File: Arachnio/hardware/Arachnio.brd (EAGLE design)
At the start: 17.8 x 58.4 mm, 64 parts, among them J5 HEAD17-NOSS, J6 HEAD17-NOSS, Q1 8MHz, T1 FDN340P/PMV48XP, U1 ATMEGA32U4-XUMU, U2 AP2111HA-3.3, U3 ZLDO1117-5.0, U5 ESP8266EX, U6 SPI_FLASH, Y1 26 MHz/10 pF

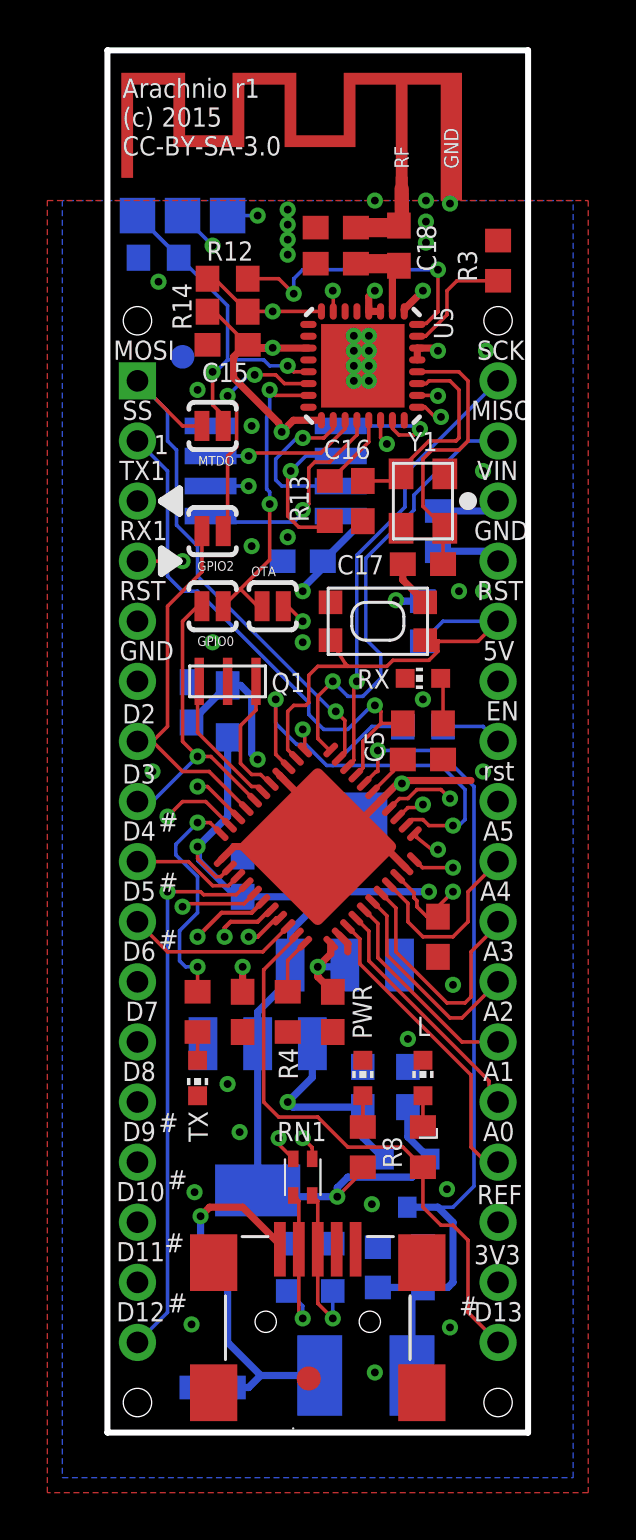
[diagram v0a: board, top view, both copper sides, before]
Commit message: -- Fixed missing parts designators in silkscreen
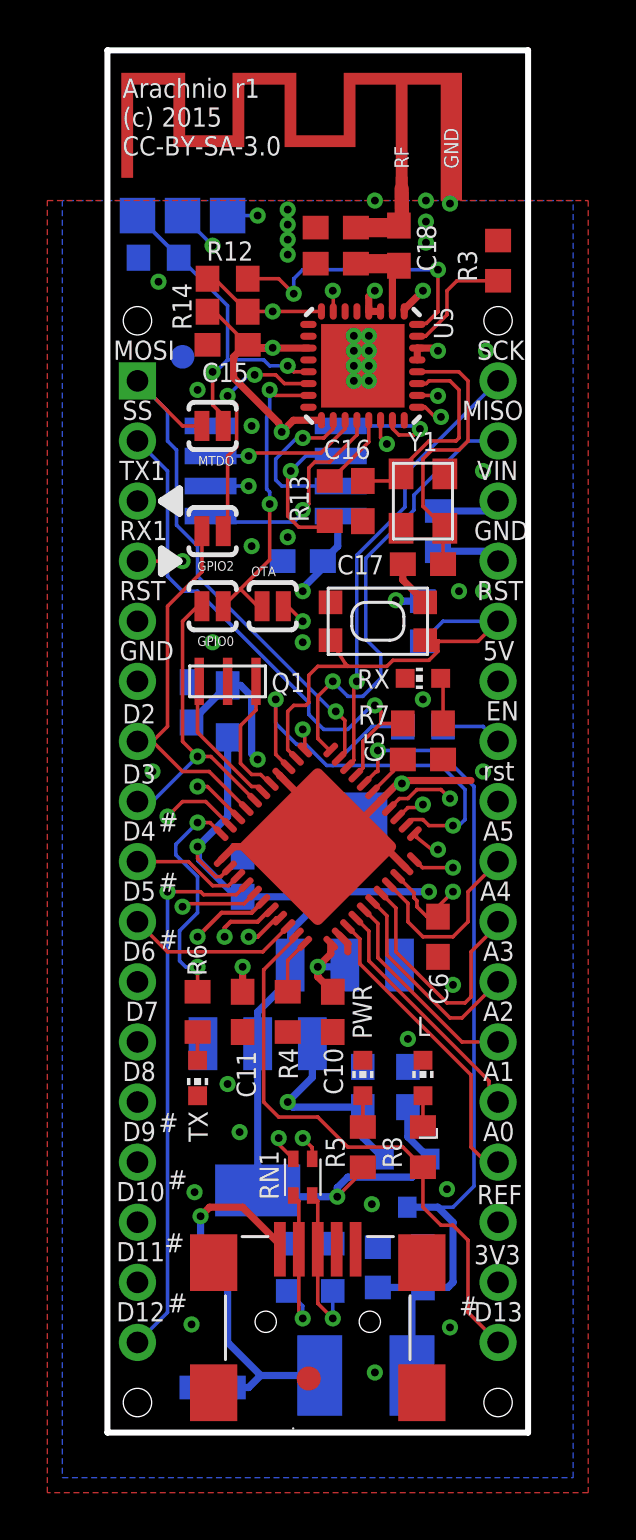
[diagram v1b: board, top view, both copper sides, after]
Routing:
- net 3V3: track 68.4 -> 66.9 mm
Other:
- board text removed: "1"

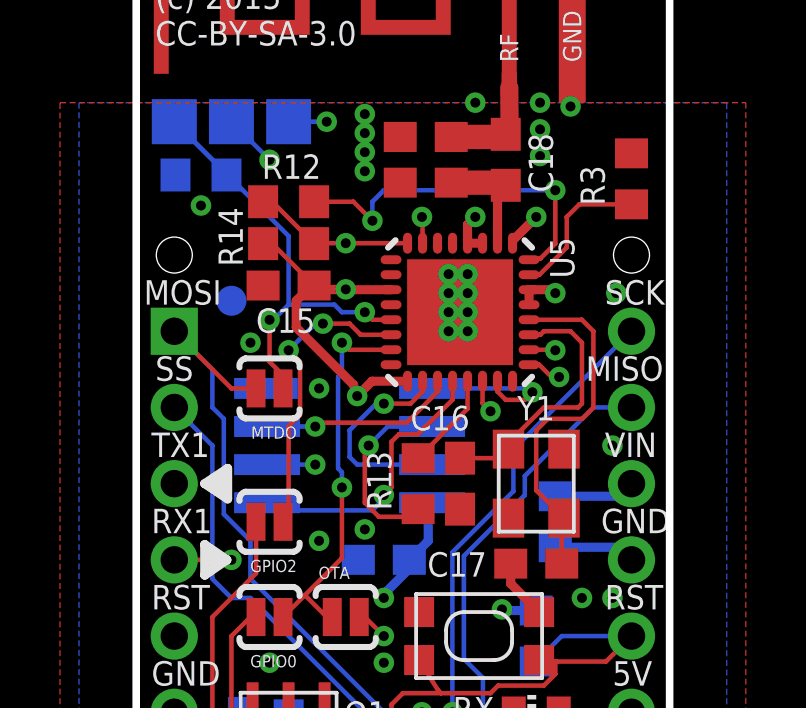
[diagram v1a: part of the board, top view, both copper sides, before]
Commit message: ﻿Added 3 new decoupling caps to the ESP8266 # Please enter the commit message for your changes. Lines starting # with '#' will be ignored, and an empty message aborts the commit. # On branch decoupling # Changes to be committed: #	modified:   Arachnio/hardware/Arachnio.brd #	modified:   Arachnio/hardware/Arachnio.sch #
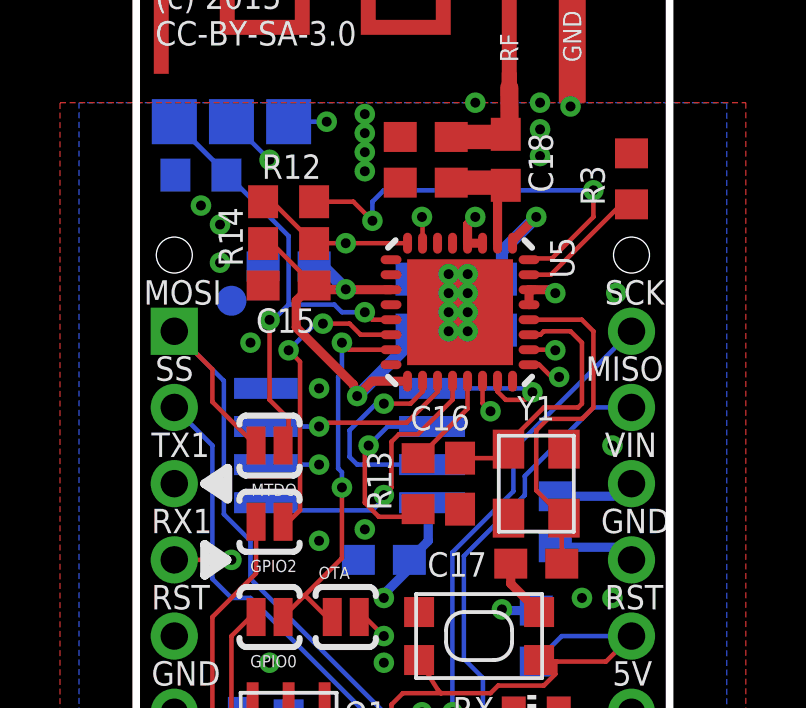
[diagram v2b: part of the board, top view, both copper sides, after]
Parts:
- added C12, C13: 100n, resistor:C0603
- added C2: 1u, resistor:C0603
- moved MTDO 1.91 mm to (4.45, 40.6)
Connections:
- net 3V3: now also C12.1, C13.1, C2.1
- net GND: now also C12.2, C13.2, C2.2
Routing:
- net 3V3: track 66.9 -> 73.7 mm
- net N$33: track 12.0 -> 14.0 mm
- net N$1: track 17.3 -> 19.2 mm
- net MOSI: track 23.3 -> 24.7 mm
- net GND: vias 38 -> 40
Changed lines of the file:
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@@
 <attribute name="BOM" value="EXCLUDE" x="4.445" y="38.1" size="1.778" layer="27" rot="R180" display="off"/>
 </element>
-<element name="MTDO" library="SparkFun-Passives" package="PAD-JUMPER-2-NO_YES_SILK" value="JUMPER-PAD-2-NOYES_SILK" x="4.445" y="42.545" rot="R180">
-<attribute name="BOM" value="EXCLUDE" x="4.445" y="42.545" size="1.778" layer="27" rot="R180" display="off"/>
+<element name="MTDO" library="SparkFun-Passives" package="PAD-JUMPER-2-NO_YES_SILK" value="JUMPER-PAD-2-NOYES_SILK" x="4.445" y="40.64" rot="R180">
+<attribute name="BOM" value="EXCLUDE" x="4.445" y="40.64" size="1.778" layer="27" rot="R180" display="off"/>
 </element>
 <element name="OTA" library="SparkFun-Passives" package="PAD-JUMPER-2-NO_YES_SILK" value="JUMPER-PAD-2-NOYES_SILK" x="6.985" y="34.925">
@@
 <element name="U$1" library="logos-faves" package="LOGO-SM" value="" x="17.145" y="46.99" rot="MR0"/>
 <element name="U$12" library="SparkFun-Aesthetics" package="OSHW-LOGO-S" value="" x="3.175" y="53.975" rot="MR0"/>
+<element name="C2" library="resistor" package="C0603" value="1u" x="5.08" y="46.609" rot="MR0">
+<attribute name="PARTNO" value="C0603C105K3PACTU" x="5.08" y="46.609" size="1.778" layer="28" rot="MR0" display="off"/>
+</element>
+<element name="C12" library="resistor" package="C0603" value="100n" x="9.144" y="45.339" rot="MR90">
+<attribute name="PARTNO" value="CC0603ZRY5V9BB104" x="9.144" y="45.339" size="1.778" layer="28" rot="MR90" display="off"/>
+</element>
+<element name="C13" library="resistor" package="C0603" value="100n" x="12.192" y="45.339" rot="MR270">
+<attribute name="PARTNO" value="CC0603ZRY5V9BB104" x="12.192" y="45.339" size="1.778" layer="28" rot="MR270" display="off"/>
+</element>
 </elements>
 <signals>
@@
 <wire x1="9.735" y1="38.73" x2="9.735" y2="37.46" width="0.3048" layer="16"/>
 <wire x1="9.735" y1="37.46" x2="9.105" y2="36.83" width="0.3048" layer="16"/>
+<contactref element="C2" pad="1"/>
+<contactref element="C12" pad="1"/>
+<contactref element="C13" pad="1"/>
+<wire x1="12.192" y1="46.189" x2="12.192" y2="47.117" width="0.4064" layer="16"/>
+<wire x1="12.192" y1="47.117" x2="13.335" y2="48.26" width="0.4064" layer="16"/>
+<wire x1="9.144" y1="44.489" x2="9.144" y2="44.069" width="0.4064" layer="16"/>
+<wire x1="9.144" y1="44.069" x2="7.366" y2="42.291" width="0.4064" layer="16"/>
+<wire x1="5.93" y1="46.609" x2="6.223" y2="46.609" width="0.4064" layer="16"/>
+<wire x1="6.223" y1="46.609" x2="6.985" y2="45.847" width="0.4064" layer="16"/>
 </signal>
 <signal name="D0/RX">
@@
 <via x="11.049" y="44.45" extent="1-16" drill="0.3302"/>
 <via x="10.414" y="44.45" extent="1-16" drill="0.3302"/>
+<contactref element="C2" pad="2"/>
+<contactref element="C12" pad="2"/>
+<contactref element="C13" pad="2"/>
+<via x="2.794" y="48.006" extent="1-16" drill="0.3302"/>
+<via x="2.794" y="46.736" extent="1-16" drill="0.3302"/>
 </signal>
 <signal name="D-">
@@
 <wire x1="3.81" y1="36.195" x2="3.81" y2="37.465" width="0.1524" layer="16"/>
 <wire x1="3.81" y1="37.465" x2="2.921" y2="38.354" width="0.1524" layer="16"/>
-<wire x1="2.921" y1="38.354" x2="2.921" y2="41.529" width="0.1524" layer="16"/>
-<wire x1="2.921" y1="41.529" x2="2.54" y2="41.91" width="0.1524" layer="16"/>
-<wire x1="2.54" y1="41.91" x2="2.54" y2="43.18" width="0.1524" layer="16"/>
-<wire x1="2.54" y1="43.18" x2="1.27" y2="44.45" width="0.1524" layer="16"/>
+<wire x1="2.921" y1="38.354" x2="2.921" y2="42.799" width="0.1524" layer="16"/>
+<wire x1="2.921" y1="42.799" x2="1.27" y2="44.45" width="0.1524" layer="16"/>
 <contactref element="MTDO" pad="2"/>
-<wire x1="3.995" y1="42.545" x2="3.175" y2="42.545" width="0.1524" layer="1"/>
-<wire x1="3.175" y1="42.545" x2="1.27" y2="44.45" width="0.1524" layer="1"/>
+<wire x1="2.54" y1="43.18" x2="1.27" y2="44.45" width="0.1524" layer="1"/>
+<wire x1="2.54" y1="43.18" x2="2.54" y2="42.095" width="0.1524" layer="1"/>
+<wire x1="2.54" y1="42.095" x2="3.995" y2="40.64" width="0.1524" layer="1"/>
 </signal>
 <signal name="D6*">
@@
 <contactref element="U5" pad="31"/>
 <contactref element="R3" pad="1"/>
-<wire x1="13.095" y1="46.335" x2="13.442" y2="46.335" width="0.1524" layer="1"/>
-<wire x1="13.442" y1="46.335" x2="14.351" y2="47.244" width="0.1524" layer="1"/>
-<wire x1="14.351" y1="47.244" x2="14.351" y2="48.26" width="0.1524" layer="1"/>
-<wire x1="14.351" y1="48.26" x2="14.771" y2="48.68" width="0.1524" layer="1"/>
-<wire x1="16.51" y1="48.68" x2="14.771" y2="48.68" width="0.1524" layer="1"/>
+<wire x1="13.095" y1="46.335" x2="13.823" y2="46.335" width="0.1524" layer="1"/>
+<wire x1="13.823" y1="46.335" x2="16.256" y2="48.768" width="0.1524" layer="1"/>
+<wire x1="16.256" y1="48.768" x2="16.256" y2="48.895" width="0.1524" layer="1"/>
+<wire x1="16.256" y1="48.895" x2="16.041" y2="48.68" width="0.1524" layer="1"/>
+<wire x1="16.51" y1="48.68" x2="16.041" y2="48.68" width="0.1524" layer="1"/>
 </signal>
 <signal name="N$33">
@@
 <contactref element="R12" pad="1"/>
 <wire x1="13.095" y1="46.835" x2="13.222" y2="46.877" width="0.1524" layer="1"/>
-<wire x1="13.222" y1="46.877" x2="13.476" y2="46.877" width="0.1524" layer="1"/>
-<wire x1="13.476" y1="46.877" x2="13.97" y2="47.371" width="0.1524" layer="1"/>
-<wire x1="13.97" y1="47.371" x2="13.97" y2="49.149" width="0.1524" layer="1"/>
-<via x="13.97" y="49.149" extent="1-16" drill="0.3302"/>
-<wire x1="13.97" y1="49.149" x2="8.255" y2="49.149" width="0.1524" layer="16"/>
+<wire x1="13.222" y1="46.877" x2="13.857" y2="46.877" width="0.1524" layer="1"/>
+<wire x1="13.857" y1="46.877" x2="15.24" y2="48.26" width="0.1524" layer="1"/>
+<via x="15.24" y="49.149" extent="1-16" drill="0.3302"/>
+<wire x1="15.24" y1="48.26" x2="15.24" y2="49.149" width="0.1524" layer="1"/>
+<wire x1="15.24" y1="49.149" x2="8.255" y2="49.149" width="0.1524" layer="16"/>
 <wire x1="8.255" y1="49.149" x2="7.874" y2="48.768" width="0.1524" layer="16"/>
 <wire x1="7.874" y1="48.768" x2="7.874" y2="48.133" width="0.1524" layer="16"/>
@@
 <wire x1="10.045" y1="42.785" x2="10.045" y2="42.43" width="0.1524" layer="1"/>
 <wire x1="10.045" y1="42.43" x2="9.017" y2="41.402" width="0.1524" layer="1"/>
-<wire x1="9.017" y1="41.402" x2="6.096" y2="41.402" width="0.1524" layer="1"/>
-<wire x1="6.096" y1="41.402" x2="5.969" y2="41.275" width="0.1524" layer="1"/>
-<via x="5.969" y="41.275" extent="1-16" drill="0.3302"/>
-<wire x1="5.969" y1="41.275" x2="4.362" y2="41.275" width="0.1524" layer="16"/>
+<wire x1="9.017" y1="41.402" x2="6.223" y2="41.402" width="0.1524" layer="1"/>
+<wire x1="6.223" y1="41.402" x2="6.096" y2="41.275" width="0.1524" layer="1"/>
+<via x="6.096" y="41.275" extent="1-16" drill="0.3302"/>
+<wire x1="6.096" y1="41.275" x2="4.362" y2="41.275" width="0.1524" layer="16"/>
 </signal>
 <signal name="N$39">
@@
 <wire x1="11.811" y1="41.783" x2="9.144" y2="41.783" width="0.1524" layer="15"/>
 <wire x1="9.144" y1="41.783" x2="8.763" y2="41.402" width="0.1524" layer="15"/>
-<wire x1="8.763" y1="41.402" x2="7.366" y2="41.402" width="0.1524" layer="15"/>
-<wire x1="7.366" y1="41.402" x2="5.969" y2="40.005" width="0.1524" layer="15"/>
-<via x="5.969" y="40.005" extent="1-16" drill="0.3302"/>
-<wire x1="5.969" y1="40.005" x2="4.362" y2="40.005" width="0.1524" layer="16"/>
+<wire x1="8.763" y1="41.402" x2="7.493" y2="41.402" width="0.1524" layer="15"/>
+<wire x1="7.493" y1="41.402" x2="6.096" y2="40.005" width="0.1524" layer="15"/>
+<via x="6.096" y="40.005" extent="1-16" drill="0.3302"/>
+<wire x1="6.096" y1="40.005" x2="4.362" y2="40.005" width="0.1524" layer="16"/>
 </signal>
 <signal name="ESP_RST">
@@
 <wire x1="4.572" y1="44.831" x2="4.445" y2="44.831" width="0.1524" layer="16"/>
 <via x="4.445" y="44.831" extent="1-16" drill="0.3302"/>
-<wire x1="4.445" y1="44.831" x2="4.445" y2="43.434" width="0.1524" layer="1"/>
-<wire x1="4.445" y1="43.434" x2="5.08" y2="42.799" width="0.1524" layer="1"/>
-<wire x1="5.08" y1="42.799" x2="5.08" y2="42.73" width="0.1524" layer="1"/>
-<wire x1="5.08" y1="42.73" x2="4.895" y2="42.545" width="0.1524" layer="1"/>
+<wire x1="4.445" y1="44.831" x2="4.445" y2="42.164" width="0.1524" layer="1"/>
+<wire x1="4.445" y1="42.164" x2="5.08" y2="41.529" width="0.1524" layer="1"/>
+<wire x1="5.08" y1="41.529" x2="5.08" y2="40.825" width="0.1524" layer="1"/>
+<wire x1="5.08" y1="40.825" x2="4.895" y2="40.64" width="0.1524" layer="1"/>
 <contactref element="TP1" pad="TP"/>
 <wire x1="5.08" y1="45.339" x2="5.08" y2="47.625" width="0.1524" layer="16"/>
@@
 <via x="5.08" y="43.815" extent="1-16" drill="0.3302"/>
 <wire x1="5.08" y1="43.815" x2="5.461" y2="43.434" width="0.1524" layer="1"/>
-<wire x1="5.461" y1="43.434" x2="5.461" y2="41.656" width="0.1524" layer="1"/>
-<wire x1="5.461" y1="41.656" x2="5.08" y2="41.275" width="0.1524" layer="1"/>
-<wire x1="5.08" y1="41.275" x2="5.08" y2="37.973" width="0.1524" layer="1"/>
+<wire x1="5.461" y1="43.434" x2="5.461" y2="38.481" width="0.1524" layer="1"/>
+<wire x1="5.461" y1="38.481" x2="5.08" y2="38.1" width="0.1524" layer="1"/>
+<wire x1="5.08" y1="38.1" x2="5.08" y2="37.973" width="0.1524" layer="1"/>
 <wire x1="5.08" y1="37.973" x2="4.953" y2="38.1" width="0.1524" layer="1"/>
 <wire x1="4.953" y1="38.1" x2="4.953" y2="38.158" width="0.1524" layer="1"/>

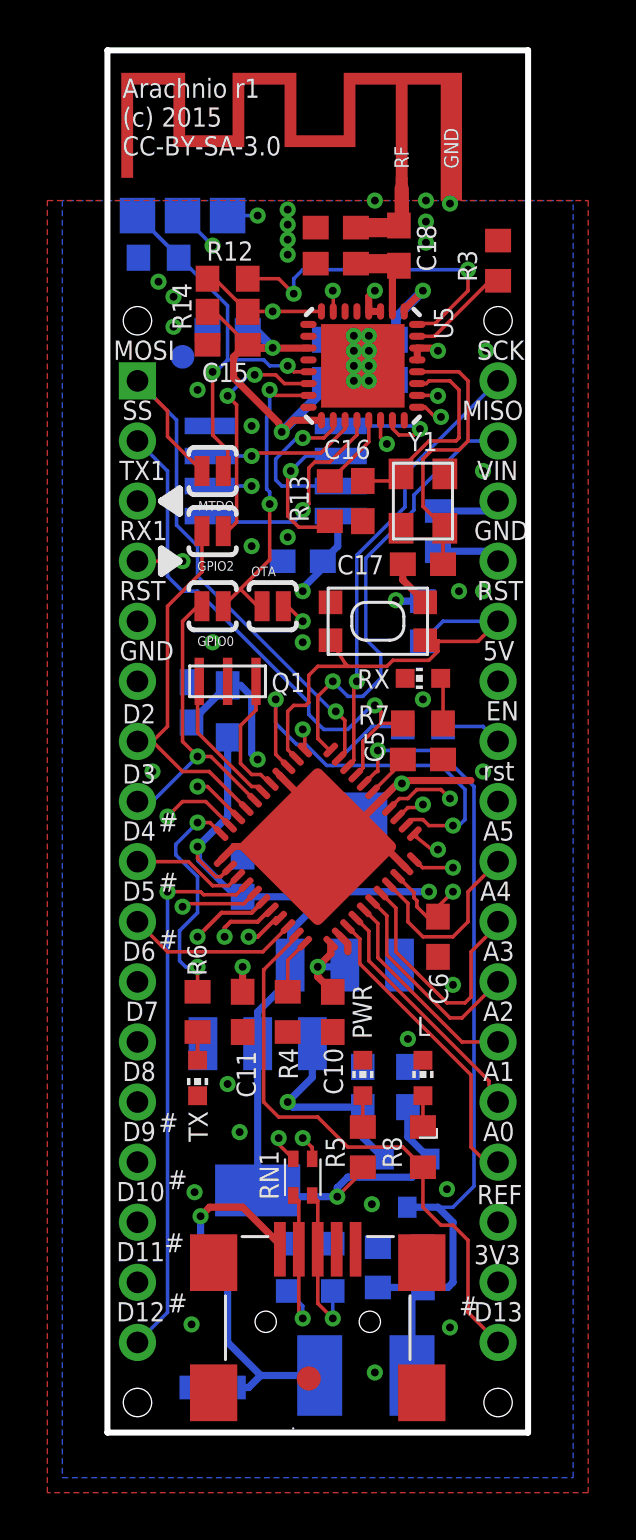
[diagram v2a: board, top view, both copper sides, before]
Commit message: -- Fixed ground plane issues -- Connected USB shield to ground -- Simplified boot select by tying MTDO and GPIO2 low and high, respectively -- Removed test points for MTDO and GPIO2 -- Replaced 0R resistor with NC by trace solder jumper -- Replaced GPIO2 and OTA jumpers with a single 3-way NO solder jumper
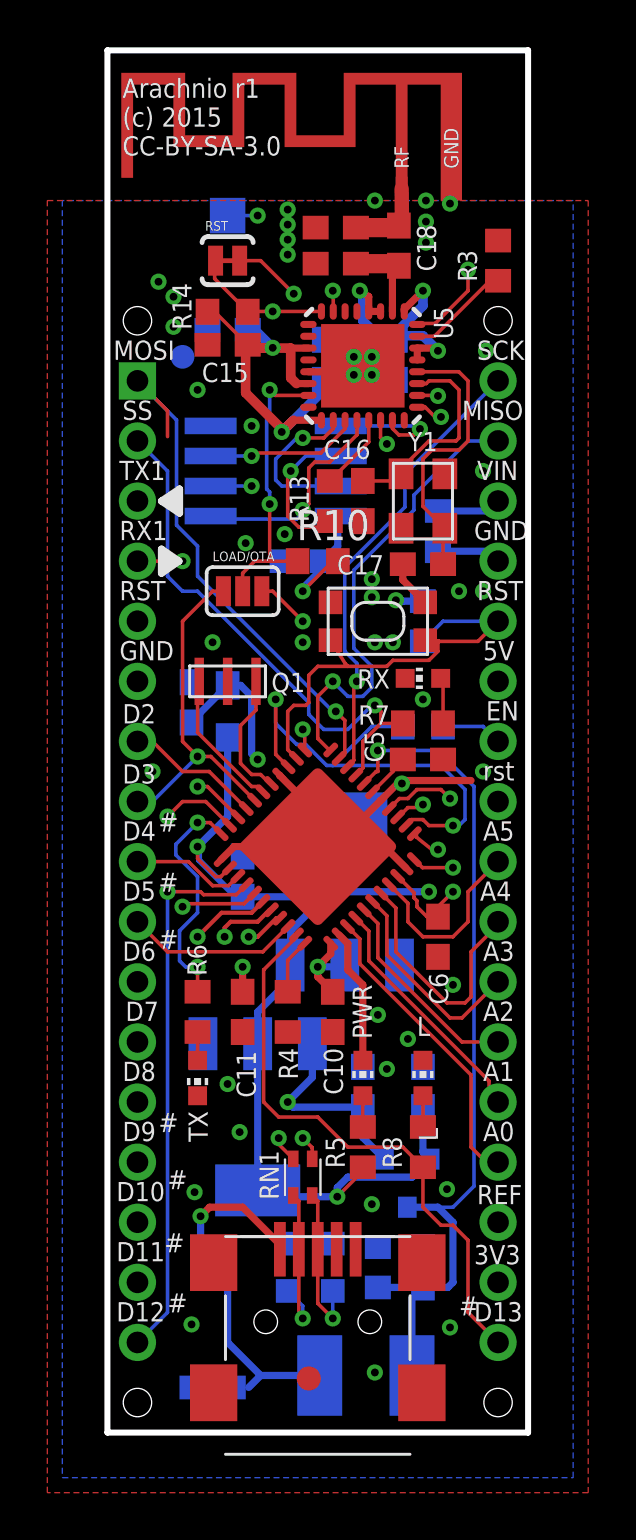
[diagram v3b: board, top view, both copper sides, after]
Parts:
- removed GPIO0, GPIO2, MTDO, OTA: JUMPER-PAD-2-NOYES_SILK, SparkFun-Passives:PAD-JUMPER-2-NO_YES_SILK
- removed R12: 0R, resistor:R0603
- removed TP1, TP2: PTR1TP15SQ, testpad:TP15SQ
- added LOAD/OTA: JUMPER-PAD-3-NOYES_SILK, SparkFun-Passives:PAD-JUMPER-3-NO_YES_SILK
- added RST: JUMPER-PAD-2-NC_BY_TRACE, SparkFun-Passives:PAD-JUMPER-2-NC_BY_TRACE_YES_SILK
- moved R10 14.5 mm to (8.89, 36.8), flipped to the top, turned to 0 degrees
- moved C3 0.64 mm to (13.3, 14.6)
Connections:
- removed net N$1: MTDO.1, R10.2, TP1.TP, U5.13
- removed net N$5: GPIO2.1, TP2.TP, U5.14
- net 3V3: now also R10.2, U5.14
- net D2/SDA: no longer GPIO2.2
- net D3/SCL: now also LOAD/OTA.3; no longer GPIO0.2
- net ESP_RST: now also RST.1; no longer R12.2
- net GND: now also CN1.GND1, CN1.GND2, CN1.GND3, CN1.GND4, U5.13; no longer R10.1
- net MOSI: no longer MTDO.2
- net N$33: now also RST.2; no longer R12.1
- net N$6: now also LOAD/OTA.2, R10.1; no longer GPIO0.1, OTA.1
- net RESET: now also LOAD/OTA.1; no longer OTA.2
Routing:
- net N$1: track 19.2 -> 0.00 mm, vias 2 -> 0
- net N$5: track 18.8 -> 0.00 mm, vias 3 -> 0
- net 3V3: track 73.7 -> 83.6 mm
- net D2/SDA: track 15.5 -> 5.77 mm
- net GND: track 27.0 -> 34.7 mm, vias 40 -> 42
- net MOSI: track 24.7 -> 22.6 mm
- net CHIP_EN: track 25.9 -> 27.2 mm
- net RESET: track 35.3 -> 36.5 mm
- net D3/SCL: track 13.6 -> 14.7 mm
- net D7: track 30.0 -> 29.1 mm
- net VUSBD: track 16.0 -> 15.4 mm
- net N$33: track 14.0 -> 14.6 mm
- net N$6: track 22.0 -> 21.3 mm
- net AREF: track 19.3 -> 18.8 mm
